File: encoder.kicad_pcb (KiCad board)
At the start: 2 copper layers, 24 x 24 mm, 7 parts, among them IC1 AS5600-ASOT, J1 BM04B-SURS-TFLFSN, SW1 A6S-2104-H

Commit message: Reworked lots
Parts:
- removed REF** (x2): MountingHole_2.7mm_M2.5_DIN965_Pad, MountingHole:MountingHole_2.7mm_M2.5_DIN965_Pad
- removed SW1: A6S-2104-H, 2_POS_DIP:A6S-2104-H
- added H1: MountingHole, MountingHole:MountingHole_2.7mm_M2.5_ISO7380, F.Cu at (-7.00, 0.00)
- added H2: MountingHole, MountingHole:MountingHole_2.7mm_M2.5_ISO7380, F.Cu at (7.00, 0.00)
- added H3: MountingHole, MountingHole:MountingHole_2.7mm_M2.5_ISO7380, F.Cu at (-28.1, -8.00)
- added R1: R, Resistor_SMD:R_0603_1608Metric_Pad0.98x0.95mm_HandSolder, F.Cu at (-3.50, 1.90)
- added R2: R, Resistor_SMD:R_0603_1608Metric_Pad0.98x0.95mm_HandSolder, F.Cu at (-3.50, -1.50)
- moved U1 95.1 mm to (0.00, 0.00), turned to 90 degrees
- moved J1 94.2 mm to (1.20, -6.65)
- moved C2 88.2 mm to (0.60, 6.40), turned to 180 degrees
- moved C1 87.4 mm to (0.60, 4.50), turned to 0 degrees
- renumbered IC1 to U1
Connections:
- net Net-(IC1-Pad7) renamed /SCL
- J1 pad 2: GND -> /SDA
- J1 pad 4: Net-(IC1-Pad6) -> GND
- U1 pad 6: Net-(IC1-Pad6) -> /SDA
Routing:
- net +3.3V: track 0.00 -> 13.5 mm, vias 0 -> 2
- net GND: track 0.00 -> 7.69 mm, vias 0 -> 2
- net /DIR: track 0.00 -> 6.46 mm
- net /SDA: track 0.00 -> 4.05 mm
- net /SCL: track 0.00 -> 4.05 mm
- added copper zone on B.Cu, net +3.3V
- added copper zone on F.Cu, net GND
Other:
- board size 24 x 24 mm -> 23 x 23 mm
- board text added: "+ve:"
- board text added: "3V3"
- board text added: "CCW"
- board text added: "CW"
- board text added: "D=23mm"
- board text added: "GND"
- board text added: "GND SCL SDA 3V3"
- board text added: "Gordon Lay Lui H-P"
- board text added: "SNEK V1.0 TWIST SENSOR"
- board text added: "TYP M2.5 D14mm"
- board text added: "dir:"

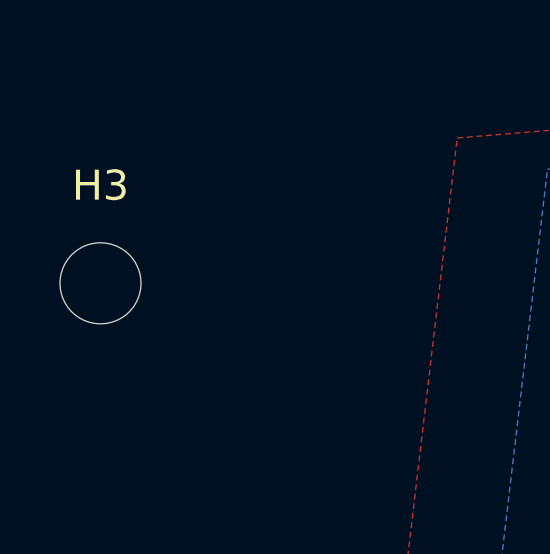
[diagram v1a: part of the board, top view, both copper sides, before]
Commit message: changed mounting hole size from M2.5 (D2.7) to D2.1
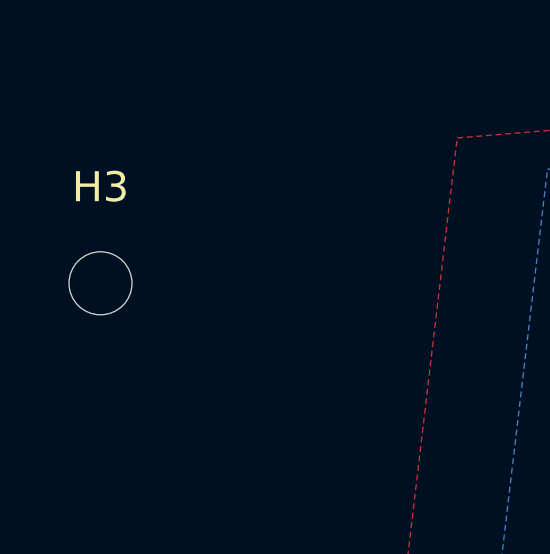
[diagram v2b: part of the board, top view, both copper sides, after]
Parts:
- H3: footprint MountingHole:MountingHole_2.7mm_M2.5_ISO7380 -> MountingHole:MountingHole_2.1mm
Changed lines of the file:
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@@
       (effects (font (size 1 1) (thickness 0.15)))
     )
+    (fp_line (start 1.6 -2.45) (end 1.6 2.45) (layer "F.SilkS") (width 0.2))
     (fp_line (start -1.6 -2.45) (end 1.6 -2.45) (layer "F.SilkS") (width 0.2))
+    (fp_line (start -1.6 2.45) (end -1.6 -2.45) (layer "F.SilkS") (width 0.2))
+    (fp_line (start -3.45 -2.58) (end -1.95 -2.58) (layer "F.SilkS") (width 0.2))
     (fp_line (start 1.6 2.45) (end -1.6 2.45) (layer "F.SilkS") (width 0.2))
-    (fp_line (start -3.45 -2.58) (end -1.95 -2.58) (layer "F.SilkS") (width 0.2))
-    (fp_line (start -1.6 2.45) (end -1.6 -2.45) (layer "F.SilkS") (width 0.2))
-    (fp_line (start 1.6 -2.45) (end 1.6 2.45) (layer "F.SilkS") (width 0.2))
+    (fp_line (start 3.7 -2.7) (end 3.7 2.7) (layer "F.Fab") (width 0.05))
+    (fp_line (start -3.7 -2.7) (end 3.7 -2.7) (layer "F.Fab") (width 0.05))
+    (fp_line (start 3.7 2.7) (end -3.7 2.7) (layer "F.Fab") (width 0.05))
+    (fp_line (start 1.95 2.45) (end -1.95 2.45) (layer "F.Fab") (width 0.1))
+    (fp_line (start -1.95 2.45) (end -1.95 -2.45) (layer "F.Fab") (width 0.1))
     (fp_line (start -3.7 2.7) (end -3.7 -2.7) (layer "F.Fab") (width 0.05))
     (fp_line (start 1.95 -2.45) (end 1.95 2.45) (layer "F.Fab") (width 0.1))
-    (fp_line (start -1.95 2.45) (end -1.95 -2.45) (layer "F.Fab") (width 0.1))
+    (fp_line (start -1.95 -2.45) (end 1.95 -2.45) (layer "F.Fab") (width 0.1))
     (fp_line (start -1.95 -1.18) (end -0.68 -2.45) (layer "F.Fab") (width 0.1))
-    (fp_line (start 3.7 2.7) (end -3.7 2.7) (layer "F.Fab") (width 0.05))
-    (fp_line (start -1.95 -2.45) (end 1.95 -2.45) (layer "F.Fab") (width 0.1))
-    (fp_line (start -3.7 -2.7) (end 3.7 -2.7) (layer "F.Fab") (width 0.05))
-    (fp_line (start 1.95 2.45) (end -1.95 2.45) (layer "F.Fab") (width 0.1))
-    (fp_line (start 3.7 -2.7) (end 3.7 2.7) (layer "F.Fab") (width 0.05))
     (pad "1" smd rect locked (at -2.7 -1.905 90) (size 1.5 0.65) (layers "F.Cu" "F.Paste" "F.Mask")
       (net 5 "+3.3V") (pinfunction "VDD5V") (pintype "bidirectional"))
@@
     )
   )
-  (footprint "MountingHole:MountingHole_2.7mm_M2.5_ISO7380" (layer "F.Cu")
+  (footprint "MountingHole:MountingHole_2.1mm" (layer "F.Cu")
     (at -28.1 -8)
-    (descr "Mounting Hole 2.7mm, no annular, M2.5, ISO7380")
-    (tags "mounting hole 2.7mm no annular m2.5 iso7380")
+    (descr "Mounting Hole 2.1mm, no annular")
+    (tags "mounting hole 2.1mm no annular")
     (property "Sheetfile" "encoder.kicad_sch")
     (property "Sheetname" "")
-    (attr exclude_from_pos_files)
-    (fp_text reference "H3" (at 0 -3.25) (layer "F.SilkS")
+    (attr exclude_from_pos_files exclude_from_bom)
+    (fp_text reference "H3" (at 0 -3.2) (layer "F.SilkS")
       (effects (font (size 1 1) (thickness 0.15)))
     )
-    (fp_text value "MountingHole" (at 0 3.25) (layer "F.Fab")
+    (fp_text value "MountingHole" (at 0 3.2) (layer "F.Fab")
       (effects (font (size 1 1) (thickness 0.15)))
     )
@@
       (effects (font (size 1 1) (thickness 0.15)))
     )
-    (fp_circle (center 0 0) (end 2.25 0) (layer "Cmts.User") (width 0.15) (fill none))
-    (fp_circle (center 0 0) (end 2.5 0) (layer "F.CrtYd") (width 0.05) (fill none))
-    (pad "" np_thru_hole circle (at 0 0) (size 2.7 2.7) (drill 2.7) (layers *.Cu *.Mask))
+    (fp_circle (center 0 0) (end 2.1 0) (layer "Cmts.User") (width 0.15) (fill none))
+    (fp_circle (center 0 0) (end 2.35 0) (layer "F.CrtYd") (width 0.05) (fill none))
+    (pad "" np_thru_hole circle (at 0 0) (size 2.1 2.1) (drill 2.1) (layers *.Cu *.Mask))
   )
   (footprint "Capacitor_SMD:C_0603_1608Metric" (layer "F.Cu")

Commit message: HD2.1mm, final design for production
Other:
- board text added: "TYP HD2.1 PCD14mm"
- board text removed: "TYP M2.5 D14mm"
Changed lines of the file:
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@@
       (outputformat 1)
       (mirror false)
-      (drillshape 1)
+      (drillshape 0)
       (scaleselection 1)
       (outputdirectory "")
@@
     (property "Sheetname" "")
     (attr exclude_from_pos_files)
-    (fp_text reference "H1" (at 0 0) (layer "F.SilkS")
+    (fp_text reference "H1" (at -3.35 -0.15 90) (layer "F.SilkS")
       (effects (font (size 1 1) (thickness 0.15)))
     )
@@
       (effects (font (size 1 1) (thickness 0.15)))
     )
-    (fp_text user "${REFERENCE}" (at 0 0) (layer "F.Fab")
+    (fp_text user "${REFERENCE}" (at -3.35 -0.15 90) (layer "F.Fab")
       (effects (font (size 1 1) (thickness 0.15)))
     )
@@
     (property "Sheetname" "")
     (attr exclude_from_pos_files)
-    (fp_text reference "H2" (at 0 0) (layer "F.SilkS")
+    (fp_text reference "H2" (at 3.375 0.025 90) (layer "F.SilkS")
       (effects (font (size 1 1) (thickness 0.15)))
     )
@@
       (effects (font (size 1 1) (thickness 0.15)))
     )
-    (fp_text user "${REFERENCE}" (at 0 0) (layer "F.Fab")
+    (fp_text user "${REFERENCE}" (at 3.375 0.025 90) (layer "F.Fab")
       (effects (font (size 1 1) (thickness 0.15)))
     )
@@
   (gr_circle (center 0 0) (end 11.5 0) (layer "Edge.Cuts") (width 0.1) (fill none))
   (gr_circle (center 0 0) (end 7 0) (layer "F.Fab") (width 0.1) (fill none))
-  (gr_text "Gordon Lay\nLui H-P" (at -2.8 -5.8 270) (layer "B.SilkS")
+  (gr_text "Gordon Lay\nLui H-P" (at -4.125 -6 270) (layer "B.SilkS")
     (effects (font (size 1 1) (thickness 0.15)) (justify mirror))
   )
-  (gr_text "TYP M2.5 D14mm" (at 5 3.4 90) (layer "B.SilkS")
+  (gr_text "TYP HD2.1 PCD14mm" (at 4.2 0.45 90) (layer "B.SilkS")
     (effects (font (size 1 1) (thickness 0.15)) (justify mirror))
   )
-  (gr_text "SNEK V1.0\nTWIST\nSENSOR" (at -2.4 4.9 270) (layer "B.SilkS")
+  (gr_text "SNEK V1.0\nTWIST\nSENSOR" (at -1.325 4.925 270) (layer "B.SilkS")
     (effects (font (size 1.5 1.5) (thickness 0.15)) (justify mirror))
   )

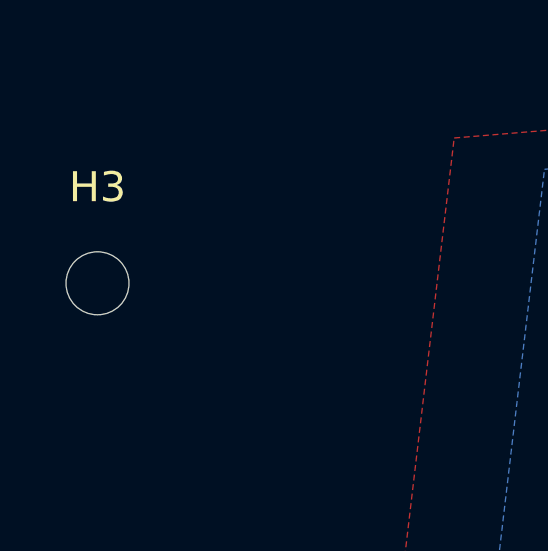
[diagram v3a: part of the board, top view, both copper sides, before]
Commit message: removed H3, regenrated gerber and drill files
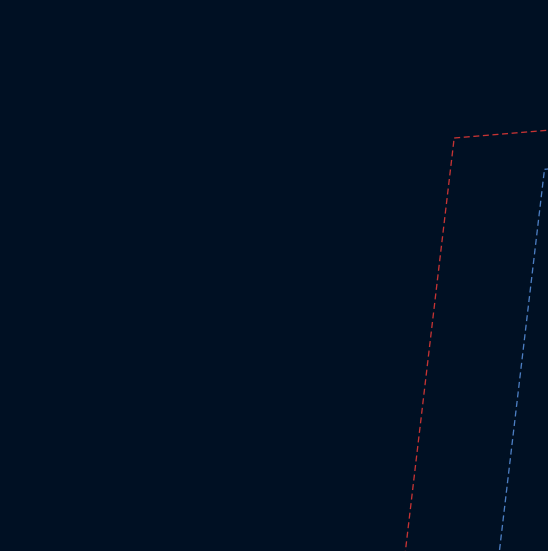
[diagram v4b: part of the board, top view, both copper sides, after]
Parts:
- removed H3: MountingHole, MountingHole:MountingHole_2.1mm
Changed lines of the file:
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@@
     )
-  )
-  (footprint "MountingHole:MountingHole_2.1mm" (layer "F.Cu")
-    (at -28.1 -8)
-    (descr "Mounting Hole 2.1mm, no annular")
-    (tags "mounting hole 2.1mm no annular")
-    (property "Sheetfile" "encoder.kicad_sch")
-    (property "Sheetname" "")
-    (attr exclude_from_pos_files exclude_from_bom)
-    (fp_text reference "H3" (at 0 -3.2) (layer "F.SilkS")
-      (effects (font (size 1 1) (thickness 0.15)))
-    )
-    (fp_text value "MountingHole" (at 0 3.2) (layer "F.Fab")
-      (effects (font (size 1 1) (thickness 0.15)))
-    )
-    (fp_text user "${REFERENCE}" (at 0 0) (layer "F.Fab")
-      (effects (font (size 1 1) (thickness 0.15)))
-    )
-    (fp_circle (center 0 0) (end 2.1 0) (layer "Cmts.User") (width 0.15) (fill none))
-    (fp_circle (center 0 0) (end 2.35 0) (layer "F.CrtYd") (width 0.05) (fill none))
-    (pad "" np_thru_hole circle (at 0 0) (size 2.1 2.1) (drill 2.1) (layers *.Cu *.Mask))
   )
   (footprint "Capacitor_SMD:C_0603_1608Metric" (layer "F.Cu")

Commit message: added frame
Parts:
- added REF**: mousebite-single-r10arc, Mousebite_straight:mousebite-single-r10arc, F.Cu at (0.00, -12.5)
- added REF**: mousebite-single-r10arc, Mousebite_straight:mousebite-single-r10arc, F.Cu at (-12.6, 0.00)
- added REF**: mousebite-single-r10arc, Mousebite_straight:mousebite-single-r10arc, F.Cu at (0.00, 12.5)
- added REF**: mousebite-single-r10arc, Mousebite_straight:mousebite-single-r10arc, F.Cu at (12.5, 0.00)
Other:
- board size 23 x 23 mm -> 40 x 40 mm
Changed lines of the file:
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@@
     )
+  )
+  (footprint "Mousebite_straight:mousebite-single-r10arc" (layer "F.Cu")
+    (at 0 -12.525)
+    (attr through_hole)
+    (fp_text reference "REF**" (at 0 -2) (layer "F.SilkS") hide
+      (effects (font (size 1 1) (thickness 0.15)))
+    )
+    (fp_text value "mousebite-single-r10arc" (at 0 2.2) (layer "F.Fab") hide
+      (effects (font (size 1 1) (thickness 0.15) italic))
+    )
+    (fp_line (start 2 1.2) (end 2 -1) (layer "Dwgs.User") (width 0.12))
+    (fp_line (start -2 -1) (end -2 1.2) (layer "Dwgs.User") (width 0.12))
+    (fp_arc (start -2.000001 1.200001) (mid -0.000001 0.998001) (end 1.999999 1.200001) (layer "Dwgs.User") (width 0.12))
+    (pad "" np_thru_hole circle (at -1.532737 0.865248) (size 0.6 0.6) (drill 0.5) (layers *.Cu *.Mask))
+    (pad "" np_thru_hole circle (at -0.768531 0.778853) (size 0.6 0.6) (drill 0.5) (layers *.Cu *.Mask))
+    (pad "" np_thru_hole circle (at 0.768531 0.778853) (size 0.6 0.6) (drill 0.5) (layers *.Cu *.Mask))
+    (pad "" np_thru_hole circle (at 0 0.75) (size 0.6 0.6) (drill 0.5) (layers *.Cu *.Mask))
+    (pad "" np_thru_hole circle (at 1.532737 0.865248) (size 0.6 0.6) (drill 0.5) (layers *.Cu *.Mask))
   )
   (footprint "AS5600:SOIC127P600X175-8N" (layer "F.Cu")
@@
     )
   )
+  (footprint "Mousebite_straight:mousebite-single-r10arc" (layer "F.Cu")
+    (at -12.55 0 90)
+    (attr through_hole)
+    (fp_text reference "REF**" (at 0 -2 90) (layer "F.SilkS") hide
+      (effects (font (size 1 1) (thickness 0.15)))
+    )
+    (fp_text value "mousebite-single-r10arc" (at 0 2.2 90) (layer "F.Fab") hide
+      (effects (font (size 1 1) (thickness 0.15) italic))
+    )
+    (fp_line (start 2 1.2) (end 2 -1) (layer "Dwgs.User") (width 0.12))
+    (fp_line (start -2 -1) (end -2 1.2) (layer "Dwgs.User") (width 0.12))
+    (fp_arc (start -2.000001 1.200001) (mid -0.000001 0.998001) (end 1.999999 1.200001) (layer "Dwgs.User") (width 0.12))
+    (pad "" np_thru_hole circle (at -1.532737 0.865248 90) (size 0.6 0.6) (drill 0.5) (layers *.Cu *.Mask))
+    (pad "" np_thru_hole circle (at -0.768531 0.778853 90) (size 0.6 0.6) (drill 0.5) (layers *.Cu *.Mask))
+    (pad "" np_thru_hole circle (at 0.768531 0.778853 90) (size 0.6 0.6) (drill 0.5) (layers *.Cu *.Mask))
+    (pad "" np_thru_hole circle (at 0 0.75 90) (size 0.6 0.6) (drill 0.5) (layers *.Cu *.Mask))
+    (pad "" np_thru_hole circle (at 1.532737 0.865248 90) (size 0.6 0.6) (drill 0.5) (layers *.Cu *.Mask))
+  )
   (footprint "Capacitor_SMD:C_0603_1608Metric" (layer "F.Cu")
     (at 0.6 4.5)
@@
     )
   )
+  (footprint "Mousebite_straight:mousebite-single-r10arc" (layer "F.Cu")
+    (at 0 12.528853 180)
+    (attr through_hole)
+    (fp_text reference "REF**" (at 0 -2) (layer "F.SilkS") hide
+      (effects (font (size 1 1) (thickness 0.15)))
+    )
+    (fp_text value "mousebite-single-r10arc" (at 0 2.2) (layer "F.Fab") hide
+      (effects (font (size 1 1) (thickness 0.15) italic))
+    )
+    (fp_line (start 2 1.2) (end 2 -1) (layer "Dwgs.User") (width 0.12))
+    (fp_line (start -2 -1) (end -2 1.2) (layer "Dwgs.User") (width 0.12))
+    (fp_arc (start -2.000001 1.200001) (mid -0.000001 0.998001) (end 1.999999 1.200001) (layer "Dwgs.User") (width 0.12))
+    (pad "" np_thru_hole circle (at -1.532737 0.865248 180) (size 0.6 0.6) (drill 0.5) (layers *.Cu *.Mask))
+    (pad "" np_thru_hole circle (at -0.768531 0.778853 180) (size 0.6 0.6) (drill 0.5) (layers *.Cu *.Mask))
+    (pad "" np_thru_hole circle (at 0.768531 0.778853 180) (size 0.6 0.6) (drill 0.5) (layers *.Cu *.Mask))
+    (pad "" np_thru_hole circle (at 0 0.75 180) (size 0.6 0.6) (drill 0.5) (layers *.Cu *.Mask))
+    (pad "" np_thru_hole circle (at 1.532737 0.865248 180) (size 0.6 0.6) (drill 0.5) (layers *.Cu *.Mask))
+  )
   (footprint "Resistor_SMD:R_0603_1608Metric_Pad0.98x0.95mm_HandSolder" (layer "F.Cu")
     (at -3.5 -1.5 90)
@@
     )
   )
+  (footprint "Mousebite_straight:mousebite-single-r10arc" (layer "F.Cu")
+    (at 12.540248 0.000001 -90)
+    (attr through_hole)
+    (fp_text reference "REF**" (at 0 -2 -270) (layer "F.SilkS") hide
+      (effects (font (size 1 1) (thickness 0.15)))
+    )
+    (fp_text value "mousebite-single-r10arc" (at 0 2.2 -270) (layer "F.Fab") hide
+      (effects (font (size 1 1) (thickness 0.15) italic))
+    )
+    (fp_line (start 2 1.2) (end 2 -1) (layer "Dwgs.User") (width 0.12))
+    (fp_line (start -2 -1) (end -2 1.2) (layer "Dwgs.User") (width 0.12))
+    (fp_arc (start -2.000001 1.200001) (mid -0.000001 0.998001) (end 1.999999 1.200001) (layer "Dwgs.User") (width 0.12))
+    (pad "" np_thru_hole circle (at -1.532737 0.865248 270) (size 0.6 0.6) (drill 0.5) (layers *.Cu *.Mask))
+    (pad "" np_thru_hole circle (at -0.768531 0.778853 270) (size 0.6 0.6) (drill 0.5) (layers *.Cu *.Mask))
+    (pad "" np_thru_hole circle (at 0.768531 0.778853 270) (size 0.6 0.6) (drill 0.5) (layers *.Cu *.Mask))
+    (pad "" np_thru_hole circle (at 0 0.75 270) (size 0.6 0.6) (drill 0.5) (layers *.Cu *.Mask))
+    (pad "" np_thru_hole circle (at 1.532737 0.865248 270) (size 0.6 0.6) (drill 0.5) (layers *.Cu *.Mask))
+  )
+  (gr_line (start 13.55 2) (end 11.325 2) (layer "Edge.Cuts") (width 0.1))
+  (gr_line (start 13.55 2) (end 13.55 13.525) (layer "Edge.Cuts") (width 0.1))
+  (gr_line (start -2 13.55) (end -13.525 13.55) (layer "Edge.Cuts") (width 0.1))
   (gr_circle (center 0 0) (end 11.5 0) (layer "Edge.Cuts") (width 0.1) (fill none))
+  (gr_line (start 13.55 13.525) (end 2 13.525) (layer "Edge.Cuts") (width 0.1))
+  (gr_rect (start -20 -20) (end 20 20) (layer "Edge.Cuts") (width 0.15) (fill none))
+  (gr_line (start 2 -13.5625) (end 2 -11.3375) (layer "Edge.Cuts") (width 0.1))
+  (gr_line (start -2 13.55) (end -2 11.325) (layer "Edge.Cuts") (width 0.1))
+  (gr_line (start 2 13.525) (end 2 11.325) (layer "Edge.Cuts") (width 0.1))
+  (gr_line (start -13.525 13.55) (end -13.525 2) (layer "Edge.Cuts") (width 0.1))
+  (gr_line (start -2 -13.525) (end -2 -11.325) (layer "Edge.Cuts") (width 0.1))
+  (gr_line (start 2 -13.5625) (end 13.525 -13.5625) (layer "Edge.Cuts") (width 0.1))
+  (gr_line (start -13.55 -2) (end -13.55 -13.525) (layer "Edge.Cuts") (width 0.1))
+  (gr_line (start -13.55 -2) (end -11.325 -2) (layer "Edge.Cuts") (width 0.1))
+  (gr_line (start 13.525 -2.0125) (end 11.325 -2.0125) (layer "Edge.Cuts") (width 0.1))
+  (gr_line (start -13.55 -13.525) (end -2 -13.525) (layer "Edge.Cuts") (width 0.1))
+  (gr_line (start 13.525 -13.5625) (end 13.525 -2.0125) (layer "Edge.Cuts") (width 0.1))
+  (gr_line (start -13.525 2) (end -11.35 2) (layer "Edge.Cuts") (width 0.1))
   (gr_circle (center 0 0) (end 7 0) (layer "F.Fab") (width 0.1) (fill none))
   (gr_text "Gordon Lay\nLui H-P" (at -4.125 -6 270) (layer "B.SilkS")
